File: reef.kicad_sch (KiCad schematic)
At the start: 1 part, among them U0 nice_nano

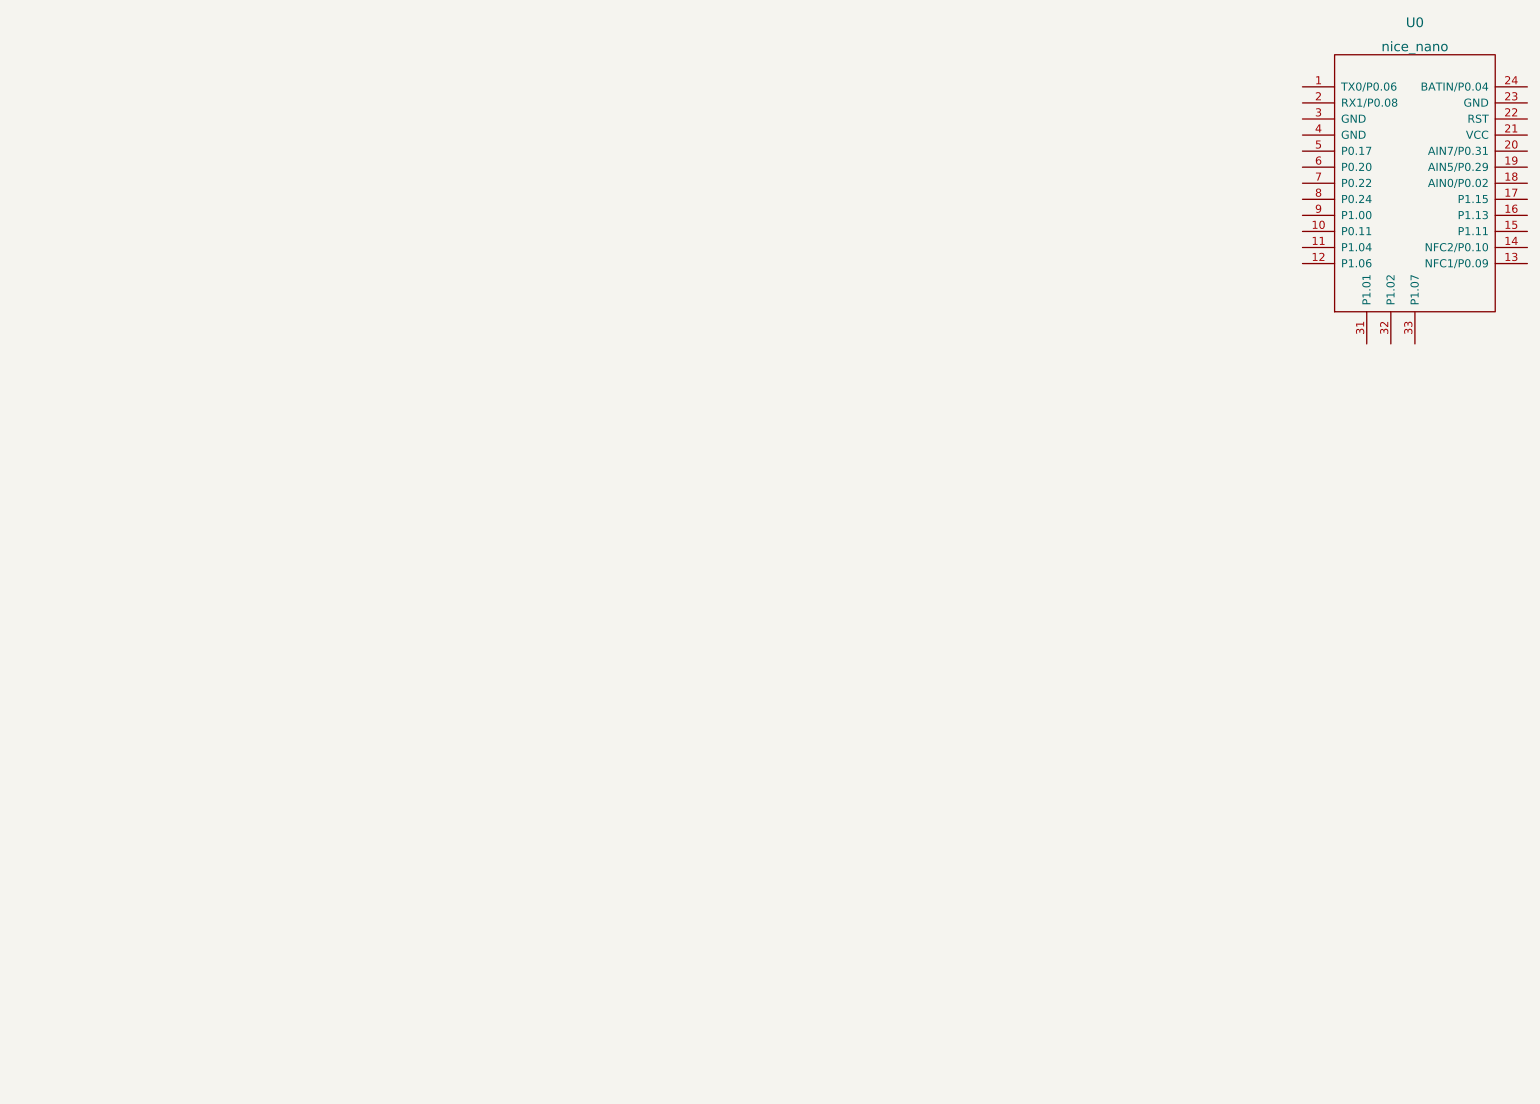
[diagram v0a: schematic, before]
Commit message: schematic complete
finished schematic, assigned footprints for most components (except connectors)
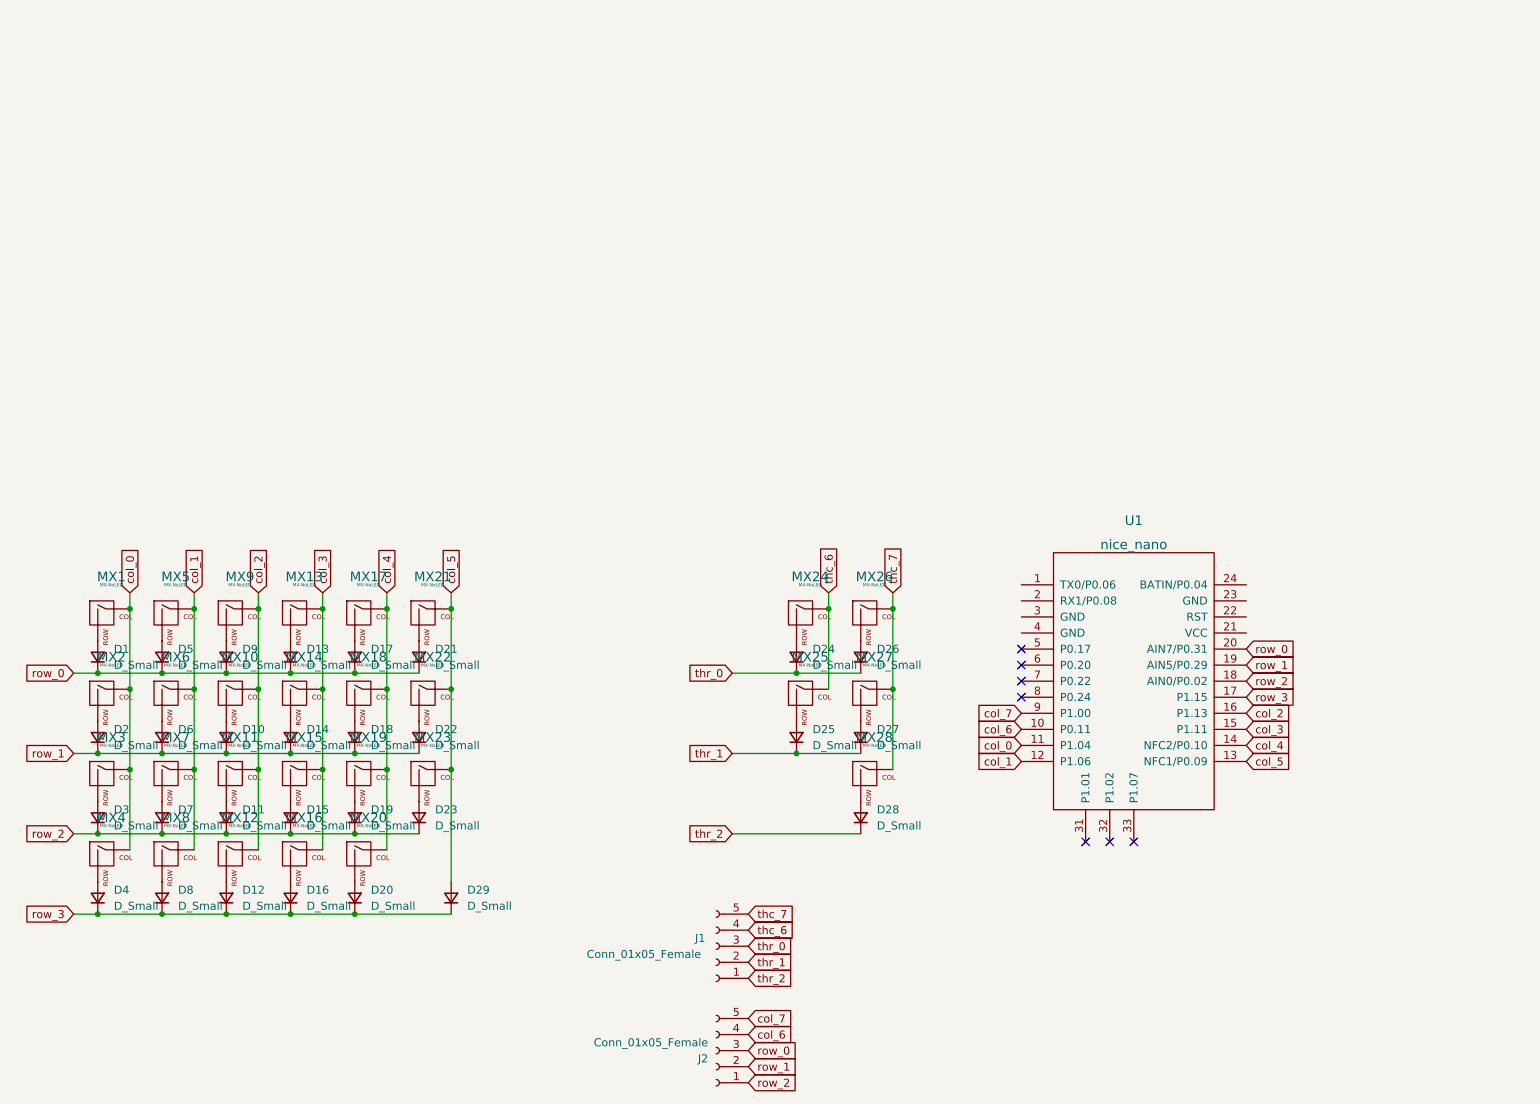
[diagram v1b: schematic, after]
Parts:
- added D1, D10, D11, D12, D13, D14, D15, D16, D17, D18, D19, D2, D20, D21, D22, D23, D24, D25, D26, D27, D28, D29, D3, D4, D5, D6, D7, D8, D9: D_Small, Diode_SMD:D_SOD-123, symbol Device:D_Small
- added J1, J2: Conn_01x05_Female, symbol Connector:Conn_01x05_Female
- added MX1, MX10, MX11, MX12, MX13, MX14, MX15, MX16, MX17, MX18, MX19, MX2, MX20, MX21, MX22, MX23, MX24, MX3, MX4, MX5, MX6, MX7, MX8, MX9: MX-NoLED, MX_Only:MXOnly-1U-Hotswap, symbol MX_Alps_Hybrid:MX-NoLED
- added MX25: MX-NoLED, MX_Only:MXOnly-2U-Hotswap, symbol MX_Alps_Hybrid:MX-NoLED
- added MX26, MX27, MX28: MX-NoLED, MX_Only:MXOnly-1.25U-Hotswap, symbol MX_Alps_Hybrid:MX-NoLED
- U1: renamed from U0; footprint (none) -> nice-nano-kicad:nice_nano
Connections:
- net col_6: now reaches U1.10 (P0.11)
- net col_6: now also J2.4 (Pin_4)
- net col_0: now reaches U1.11 (P1.04)
- net col_0: now also MX1.1 (COL), MX2.1 (COL), MX3.1 (COL), MX4.1 (COL)
- net col_1: now reaches U1.12 (P1.06)
- net col_1: now also MX5.1 (COL), MX6.1 (COL), MX7.1 (COL), MX8.1 (COL)
- net col_5: now reaches U1.13 (NFC1/P0.09)
- net col_5: now also D29.2 (A), MX21.1 (COL), MX22.1 (COL), MX23.1 (COL)
- net col_4: now reaches U1.14 (NFC2/P0.10)
- net col_4: now also MX17.1 (COL), MX18.1 (COL), MX19.1 (COL), MX20.1 (COL)
- net col_3: now reaches U1.15 (P1.11)
- net col_3: now also MX13.1 (COL), MX14.1 (COL), MX15.1 (COL), MX16.1 (COL)
- net col_2: now reaches U1.16 (P1.13)
- net col_2: now also MX10.1 (COL), MX11.1 (COL), MX12.1 (COL), MX9.1 (COL)
- net row_3: now reaches U1.17 (P1.15)
- net row_3: now also D12.1 (K), D16.1 (K), D20.1 (K), D29.1 (K), D4.1 (K), D8.1 (K)
- net row_2: now reaches U1.18 (AIN0/P0.02)
- net row_2: now also D11.1 (K), D15.1 (K), D19.1 (K), D23.1 (K), D3.1 (K), D7.1 (K), J2.1 (Pin_1)
- net row_1: now reaches U1.19 (AIN5/P0.29)
- net row_1: now also D10.1 (K), D14.1 (K), D18.1 (K), D2.1 (K), D22.1 (K), D6.1 (K), J2.2 (Pin_2)
- net row_0: now reaches U1.20 (AIN7/P0.31)
- net row_0: now also D1.1 (K), D13.1 (K), D17.1 (K), D21.1 (K), D5.1 (K), D9.1 (K), J2.3 (Pin_3)
- net col_7: now reaches U1.9 (P1.00)
- net col_7: now also J2.5 (Pin_5)
- new net: D16.2 (A), MX16.2 (ROW)
- new net: D9.2 (A), MX9.2 (ROW)
- new net: D14.2 (A), MX14.2 (ROW)
- new net: D1.2 (A), MX1.2 (ROW)
- new net: D7.2 (A), MX7.2 (ROW)
- new net: D8.2 (A), MX8.2 (ROW)
- new net: D17.2 (A), MX17.2 (ROW)
- new net: D5.2 (A), MX5.2 (ROW)
- new net: D18.2 (A), MX18.2 (ROW)
- new net: D26.2 (A), MX26.2 (ROW)
- new net: D11.2 (A), MX11.2 (ROW)
- new net: D23.2 (A), MX23.2 (ROW)
- new net: D2.2 (A), MX2.2 (ROW)
- new net: D20.2 (A), MX20.2 (ROW)
- new net: D25.2 (A), MX25.2 (ROW)
- new net: D28.2 (A), MX28.2 (ROW)
- new net: D4.2 (A), MX4.2 (ROW)
- new net: D27.2 (A), MX27.2 (ROW)
- new net: D13.2 (A), MX13.2 (ROW)
- new net: D10.2 (A), MX10.2 (ROW)
- new net: D19.2 (A), MX19.2 (ROW)
- new net: D15.2 (A), MX15.2 (ROW)
- new net: D22.2 (A), MX22.2 (ROW)
- new net: D3.2 (A), MX3.2 (ROW)
- new net: D24.2 (A), MX24.2 (ROW)
- new net: D21.2 (A), MX21.2 (ROW)
- new net: D12.2 (A), MX12.2 (ROW)
- new net: D6.2 (A), MX6.2 (ROW)
- new net thc_6: J1.4 (Pin_4), MX24.1 (COL), MX25.1 (COL)
- new net thc_7: J1.5 (Pin_5), MX26.1 (COL), MX27.1 (COL), MX28.1 (COL)
- new net thr_0: D24.1 (K), D26.1 (K), J1.3 (Pin_3)
- new net thr_1: D25.1 (K), D27.1 (K), J1.2 (Pin_2)
- new net thr_2: D28.1 (K), J1.1 (Pin_1)
- no-connect marks 0 -> 7
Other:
- moved on the sheet: U1

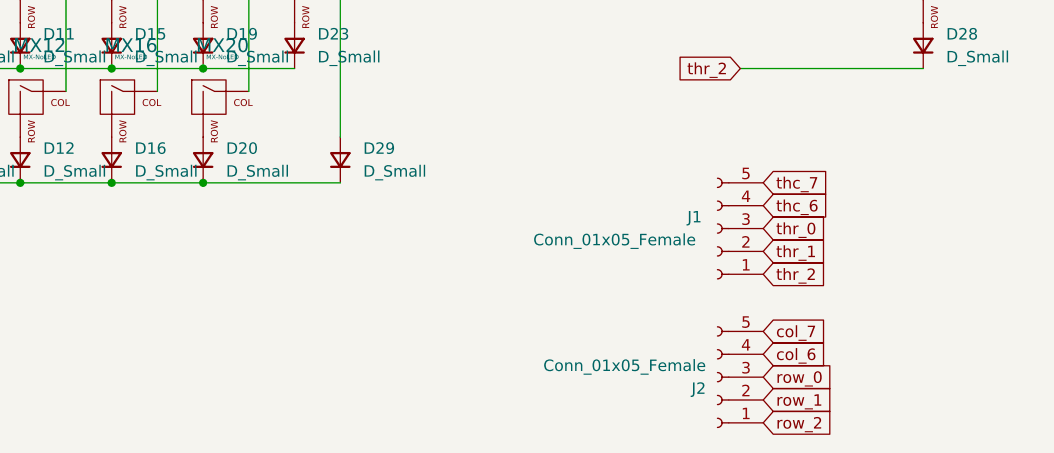
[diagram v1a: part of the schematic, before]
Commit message: update connectors
update board and thumb cluster conectors (using SF7381-5PG-3ES 5 pin panel mount connector)
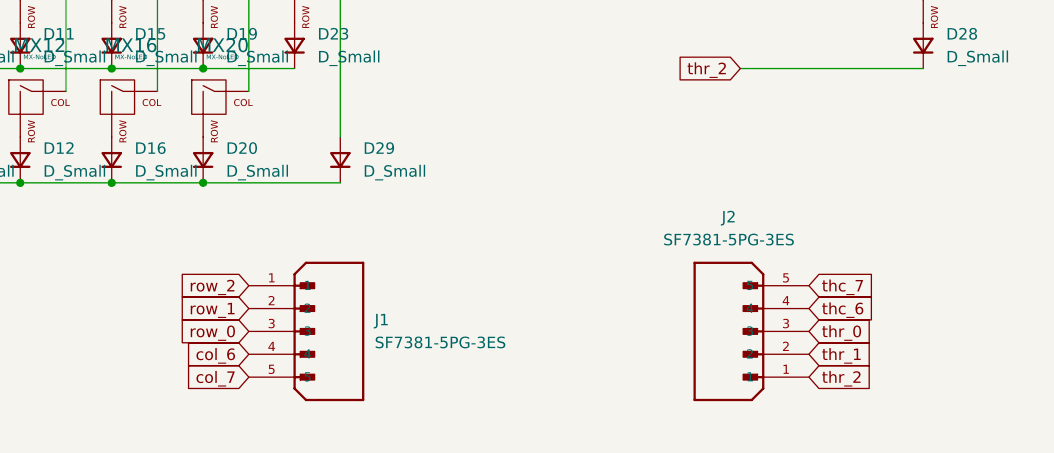
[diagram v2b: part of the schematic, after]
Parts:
- removed J1, J2: Conn_01x05_Female, symbol Connector:Conn_01x05_Female
- added J1, J2: SF7381-5PG-3ES, SF7381-5PG-3ES:SWITCHCRAFT_SF7381-5PG-3ES, symbol SF7381-5PG-3ES:SF7381-5PG-3ES
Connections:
- net col_6: now also J1.4
- net col_7: now also J1.5
- net row_0: now also J1.3
- net row_1: now also J1.2
- net row_2: now also J1.1
- net thc_6: now also J2.4
- net thc_7: now also J2.5
- net thr_0: now also J2.3
- net thr_1: now also J2.2
- net thr_2: now also J2.1

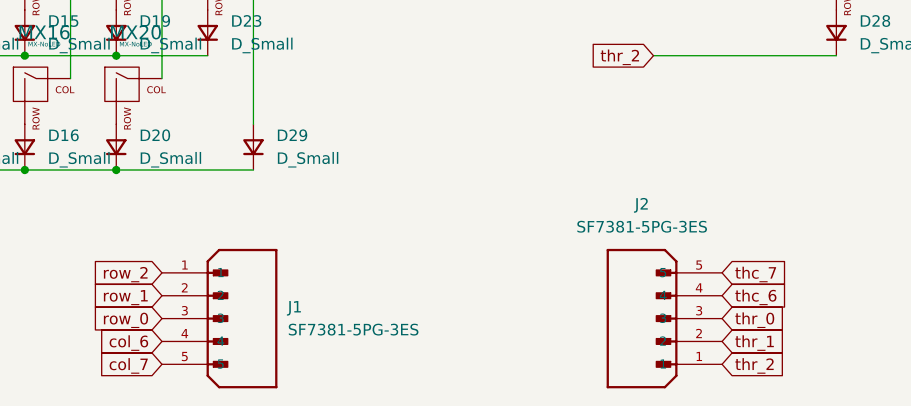
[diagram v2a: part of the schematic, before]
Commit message: Connector Change
switching to slightly smaller T4140012051-000 connector.
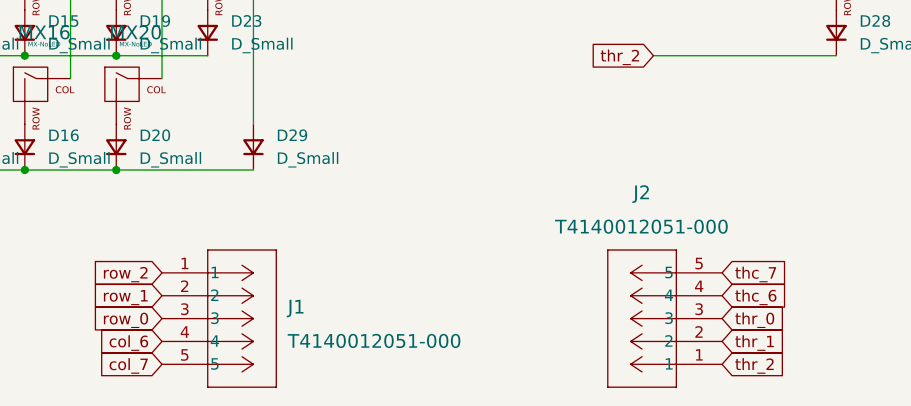
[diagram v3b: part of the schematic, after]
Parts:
- removed J1, J2: SF7381-5PG-3ES, SF7381-5PG-3ES:SWITCHCRAFT_SF7381-5PG-3ES, symbol SF7381-5PG-3ES:SF7381-5PG-3ES
- added J1, J2: T4140012051-000, footprints:CONN5_T4140012051_TEC, symbol 2023-08-20_16-16-57:T4140012051-000
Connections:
- net col_6: now also J1.4
- net col_7: now also J1.5
- net row_0: now also J1.3
- net row_1: now also J1.2
- net row_2: now also J1.1
- net thc_6: now also J2.4
- net thc_7: now also J2.5
- net thr_0: now also J2.3
- net thr_1: now also J2.2
- net thr_2: now also J2.1

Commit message: PCB updates + importing keebio library
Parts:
- D1, D10, D11, D12, D13, D14, D15, D16, D17, D18, D19, D2, D20, D21, D22, D23, D24, D25, D26, D27, D28, D29, D3, D4, D5, D6, D7, D8, D9: footprint Diode_SMD:D_SOD-123 -> modified_footprints:D_SOD-123_reversible
